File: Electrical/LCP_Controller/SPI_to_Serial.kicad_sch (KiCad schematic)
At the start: 20 parts, among them J15 SALEAE_TEST, J16 SALEAE_TEST, J17 SALEAE_TEST, J18 SALEAE_TEST, J19 SALEAE_TEST, J20 SALEAE_TEST, Q11 TSM500P02CX RFG, U15 MAX14830, Y3 4MHz

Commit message: Hardware Revision : v0.3
1. modified schematic design, removed unnecessary test points.
2. pcb layout 2x8 Inches allowance dimension, layout is in progress
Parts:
- removed TP11, TP56: 5002, TestPoint:TestPoint_Keystone_5000-5004_Miniature, symbol Connector:TestPoint
- removed TP12, TP57: 5001, TestPoint:TestPoint_Keystone_5000-5004_Miniature, symbol Connector:TestPoint
- removed TP58: 5004, TestPoint:TestPoint_Keystone_5000-5004_Miniature, symbol Connector:TestPoint
- renumbered C47 to C30, C48 to C31, C49 to C32, C50 to C33, J18 to J11, J20 to J12, J15 to J13, J17 to J14, J19 to J15, JP9 to JP8, Q11 to Q9, R27 to R23, U15 to U9, Y3 to Y2

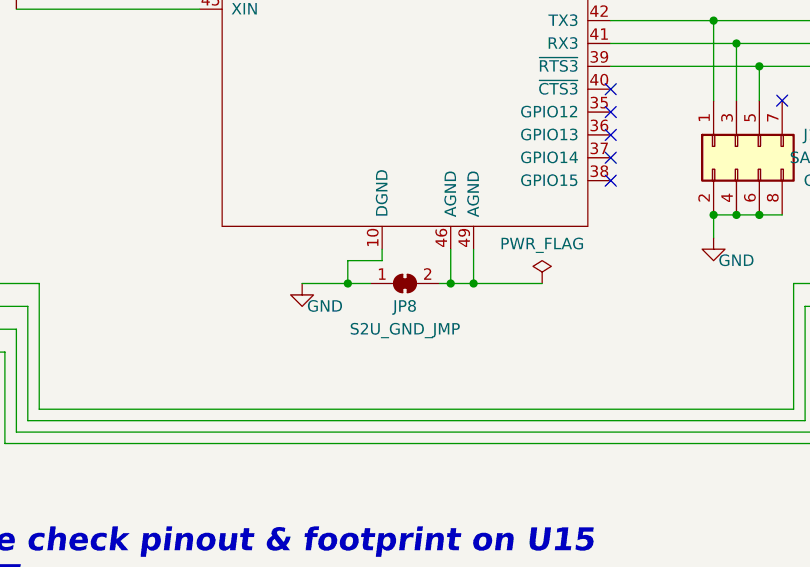
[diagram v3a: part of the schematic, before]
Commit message: Removed RF Switch
Deleted the RF Switch.

GPS Signal is routed to J17 and Iridium to J18.
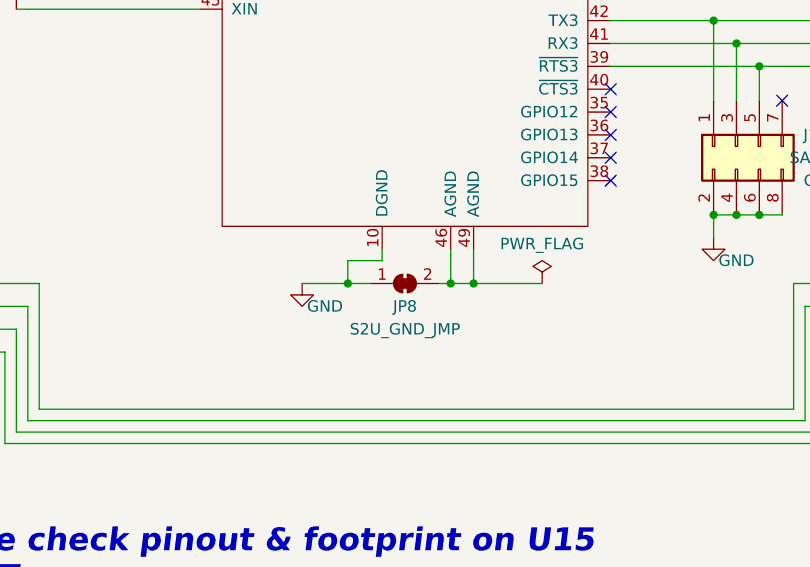
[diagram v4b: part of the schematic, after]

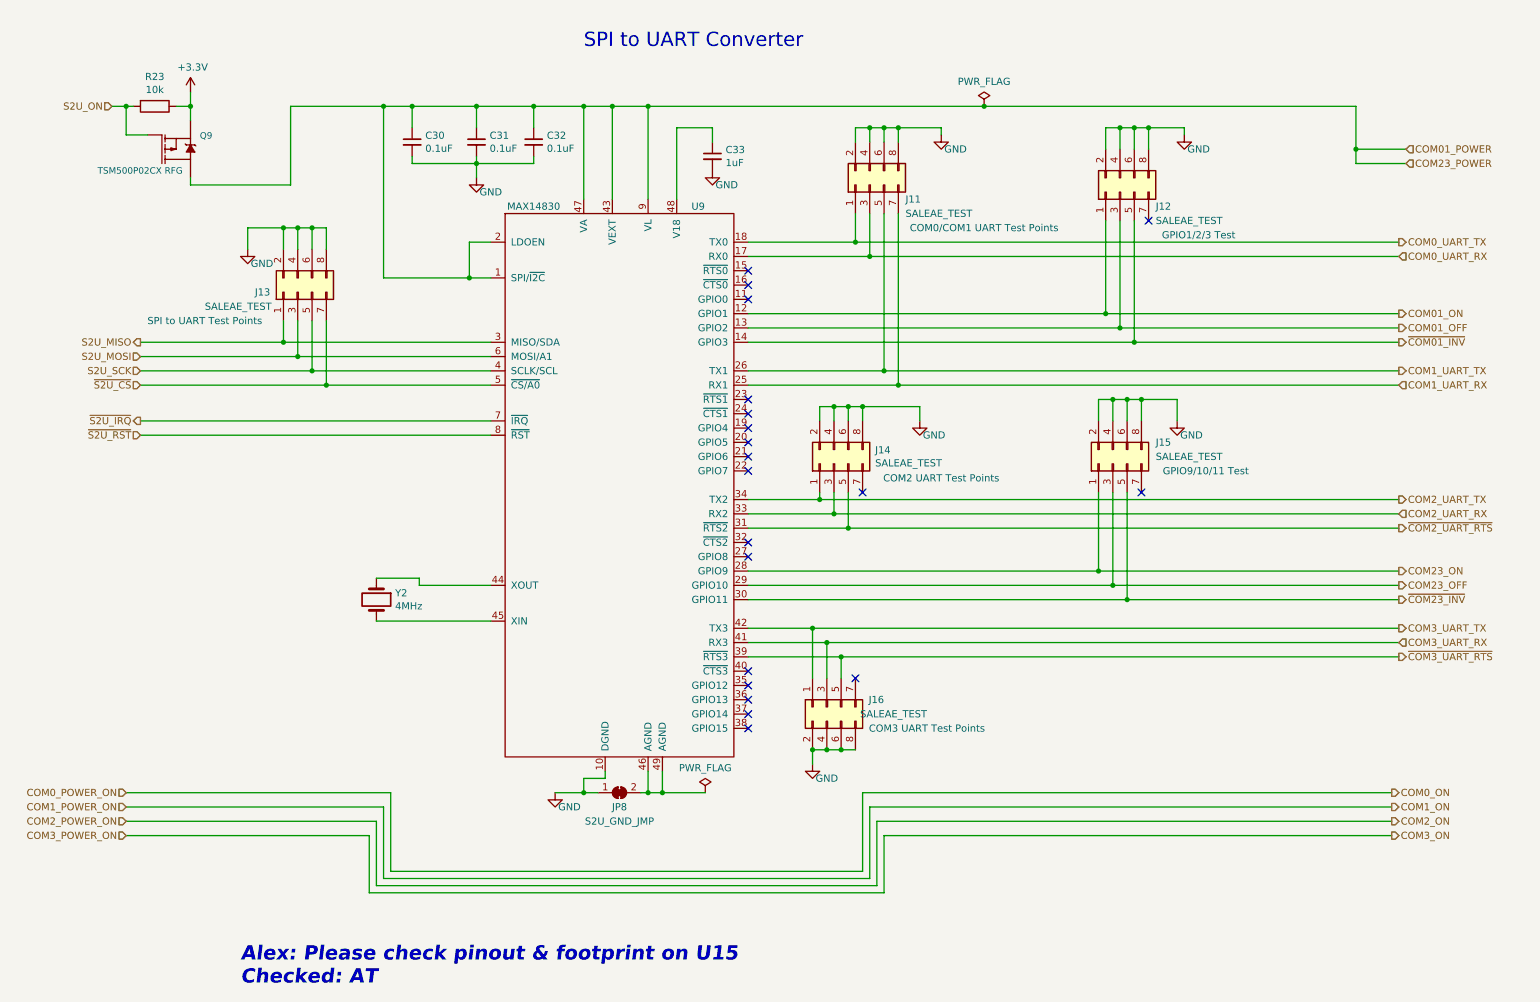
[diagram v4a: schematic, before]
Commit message: Connector Progress
J2 J22 and J23 converted to Molex Microfit

SALEAE TEST connectors removed
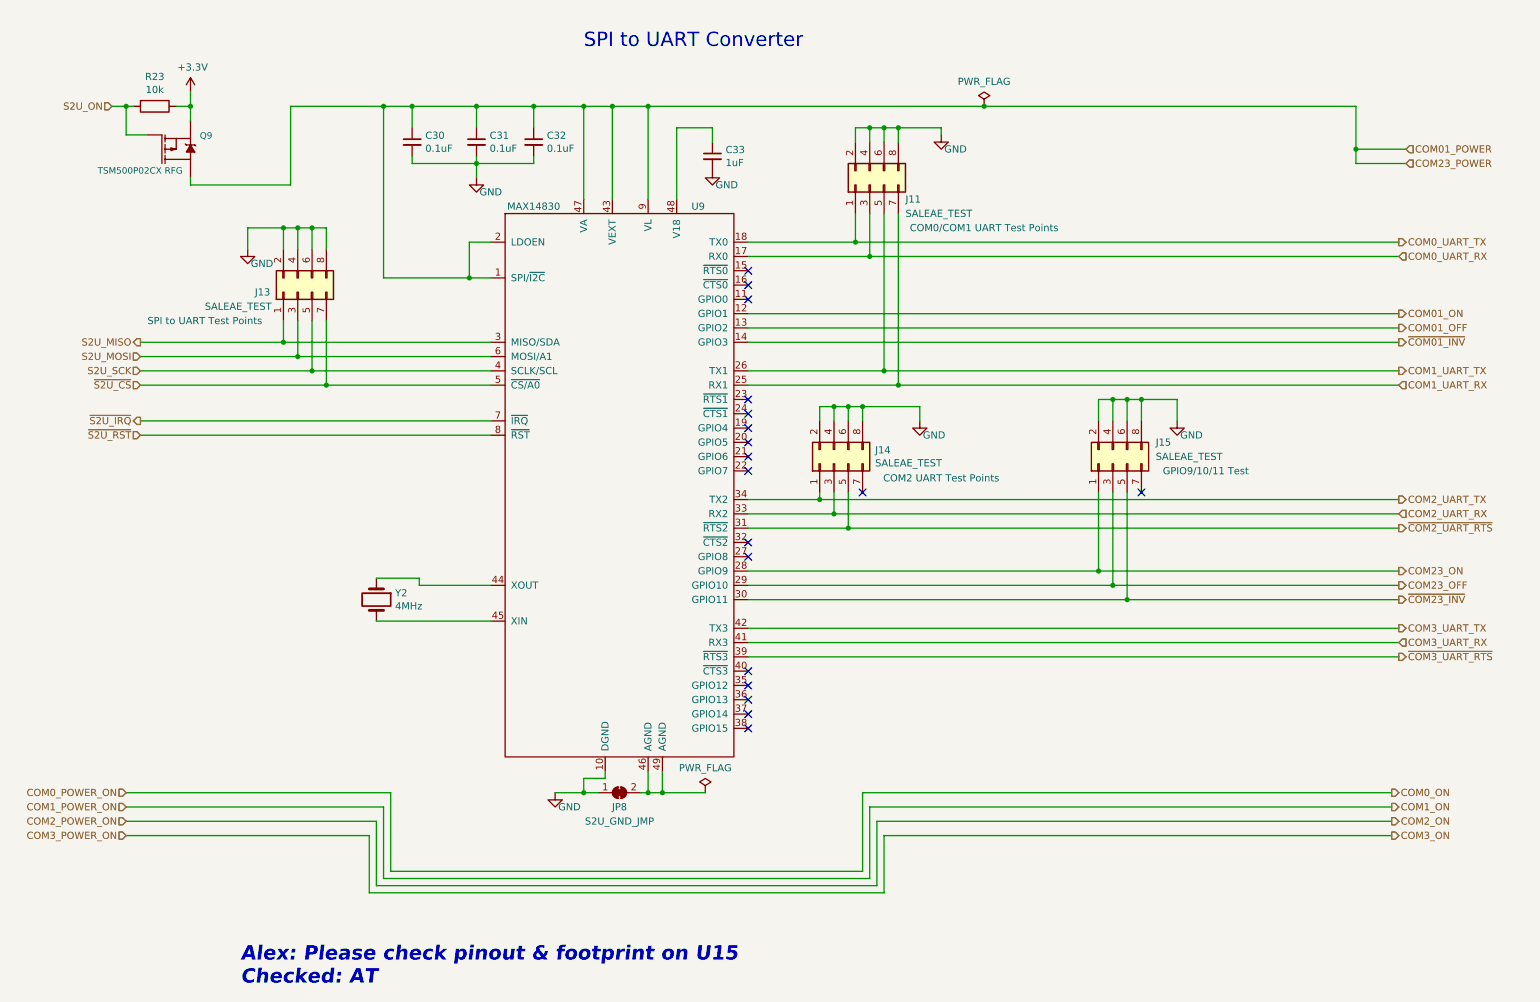
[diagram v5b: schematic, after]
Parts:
- removed J12, J16: SALEAE_TEST, Connector_PinHeader_2.54mm:PinHeader_2x04_P2.54mm_Vertical, symbol Connector_Generic:Conn_02x04_Odd_Even
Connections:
- no-connect marks 20 -> 18

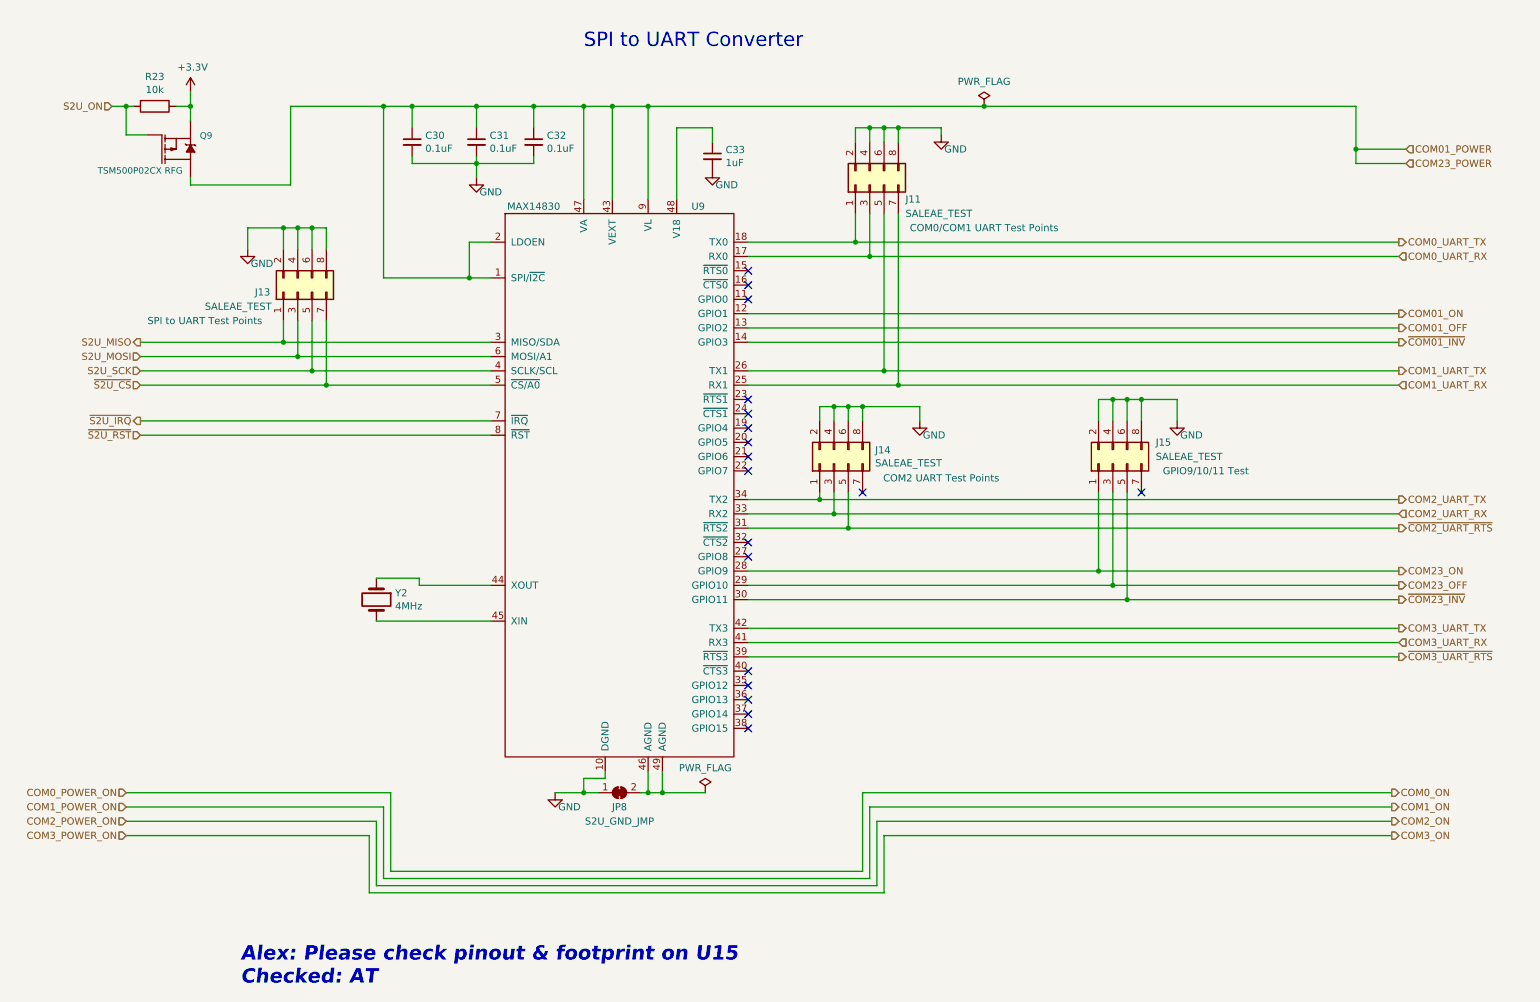
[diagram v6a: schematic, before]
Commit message: Removed the rest of the test ports
Layout updates
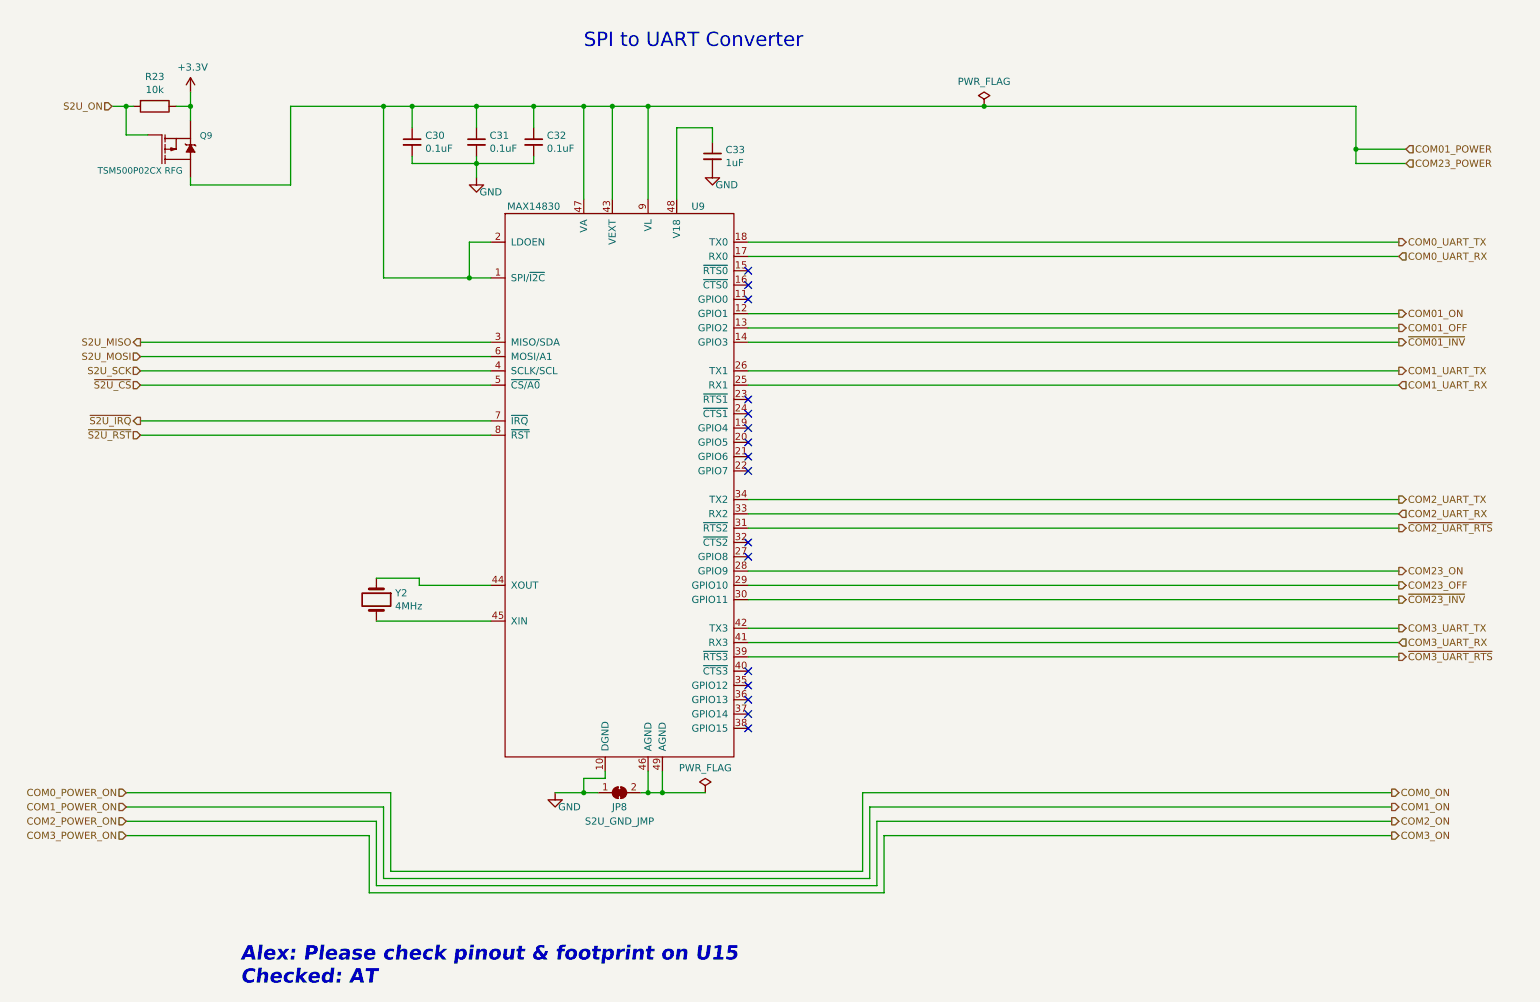
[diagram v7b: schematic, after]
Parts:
- removed J11, J13, J14, J15: SALEAE_TEST, Connector_PinHeader_2.54mm:PinHeader_2x04_P2.54mm_Vertical, symbol Connector_Generic:Conn_02x04_Odd_Even
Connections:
- no-connect marks 18 -> 16
